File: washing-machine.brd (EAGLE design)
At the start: 108.1 x 85.8 mm, 57 parts, among them IC1 MEGA8-P, IC2 7805TV, K1 ZNS5106, K2 ZNS5106, K3 ZNS5106, Q2 BC547, Q3 BC547, Q4 BC547, Q5 BC547, Q6 BC547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

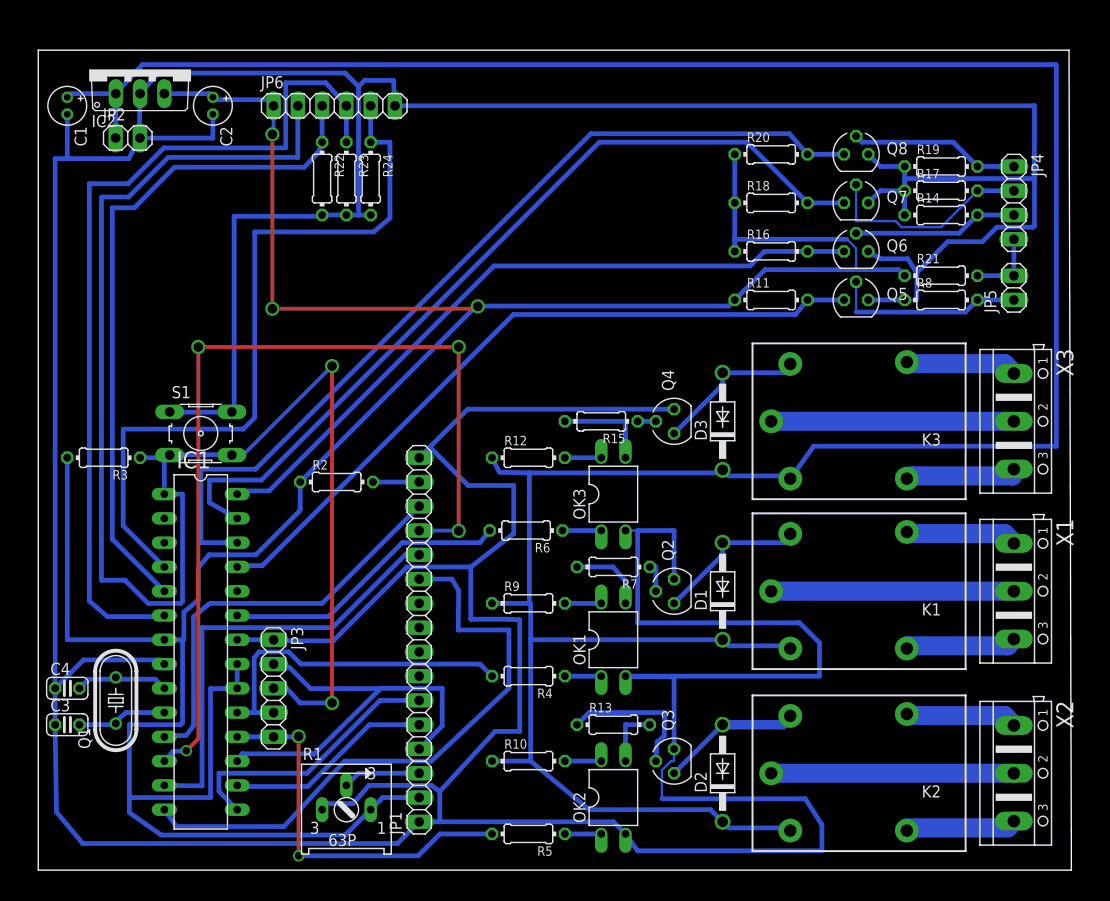
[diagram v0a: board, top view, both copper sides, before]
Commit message: Mounting holes added
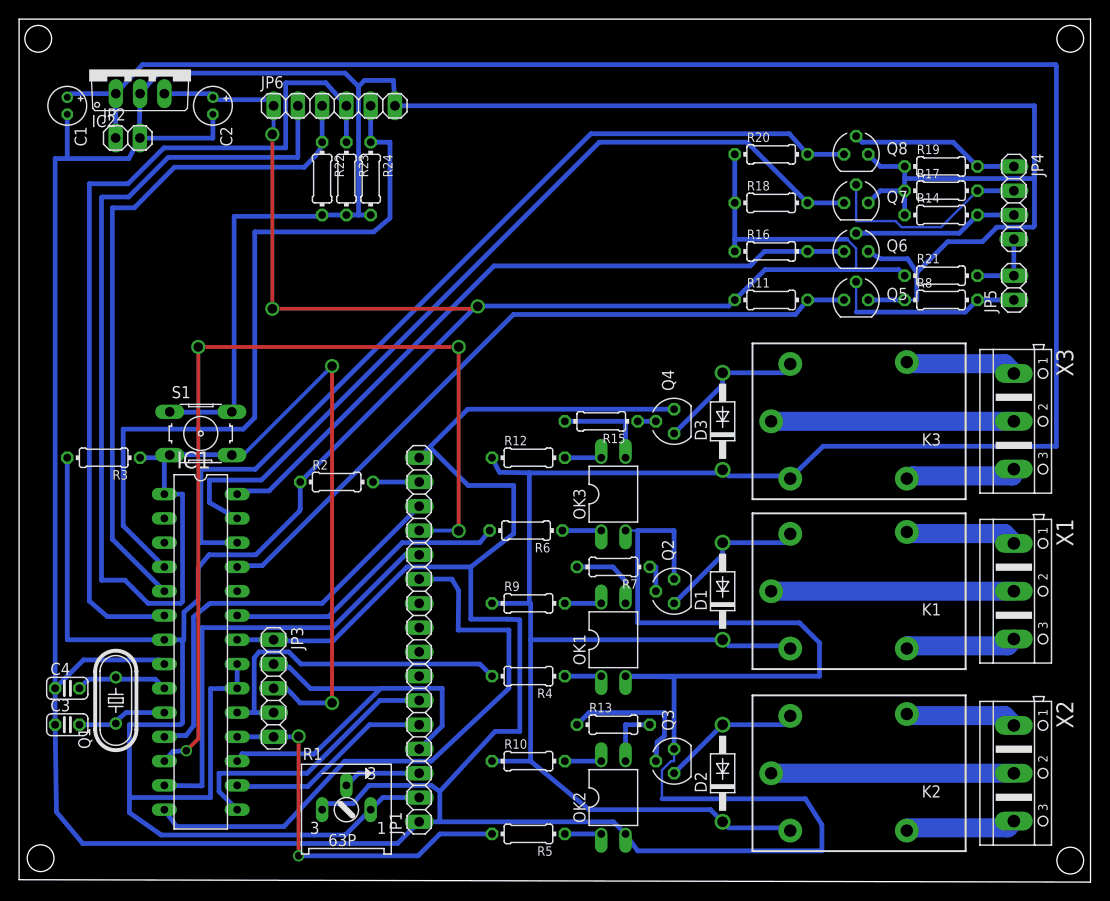
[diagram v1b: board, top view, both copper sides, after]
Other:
- board size 108.1 x 85.8 mm -> 112.1 x 90.3 mm
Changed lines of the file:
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@@
 <board>
 <plain>
-<wire x1="-0.5" y1="-1.25" x2="107.62" y2="-1.25" width="0" layer="20"/>
-<wire x1="107.62" y1="-1.25" x2="107.37" y2="84.56" width="0" layer="20"/>
-<wire x1="107.37" y1="84.56" x2="-0.5" y2="84.56" width="0" layer="20"/>
-<wire x1="-0.5" y1="84.56" x2="-0.5" y2="-1.25" width="0" layer="20"/>
+<wire x1="-2.5" y1="-2.25" x2="109.62" y2="-2.5" width="0" layer="20"/>
+<wire x1="109.62" y1="-2.5" x2="109.62" y2="87.81" width="0" layer="20"/>
+<wire x1="109.62" y1="87.81" x2="-2.5" y2="87.81" width="0" layer="20"/>
+<wire x1="-2.5" y1="87.81" x2="-2.5" y2="-2.25" width="0" layer="20"/>
+<hole x="-0.25" y="0" drill="2.8"/>
+<hole x="-0.5" y="85.75" drill="2.8"/>
+<hole x="107.5" y="85.75" drill="2.8"/>
+<hole x="107.5" y="-0.25" drill="2.8"/>
 </plain>
 <attributes>
@@
 <wire x1="106.045" y1="82.89" x2="105.98" y2="83.05" width="0.5" layer="16"/>
 <wire x1="106.045" y1="43.1125" x2="106.045" y2="82.89" width="0.5" layer="16"/>
-<wire x1="80.645" y1="43.1125" x2="106.045" y2="43.1125" width="0.5" layer="16"/>
-<wire x1="78.4225" y1="40.005" x2="80.645" y2="43.1125" width="0.5" layer="16"/>
+<wire x1="81.645" y1="43.1125" x2="106.045" y2="43.1125" width="0.5" layer="16"/>
+<wire x1="78.4225" y1="40.005" x2="81.645" y2="43.1125" width="0.5" layer="16"/>
 <wire x1="78.4225" y1="40.005" x2="78.2" y2="39.72" width="0.5" layer="16"/>
 </signal>
@@
 <contactref element="D2" pad="A"/>
 <wire x1="71.12" y1="13.97" x2="66.04" y2="8.89" width="0.5" layer="16"/>
-<wire x1="77.47" y1="13.97" x2="78.105" y2="14.605" width="0.254" layer="16"/>
-<wire x1="71.12" y1="13.97" x2="77.47" y2="13.97" width="1" layer="16"/>
-<wire x1="78.105" y1="14.605" x2="78.2" y2="14.89" width="1" layer="16"/>
+<wire x1="77.47" y1="13.97" x2="78.105" y2="14.605" width="0.5" layer="16"/>
+<wire x1="71.12" y1="13.97" x2="77.47" y2="13.97" width="0.5" layer="16"/>
+<wire x1="78.105" y1="14.605" x2="78.2" y2="14.89" width="0.5" layer="16"/>
 </signal>
 <signal name="N$19">
